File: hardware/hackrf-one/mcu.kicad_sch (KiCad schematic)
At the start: 134 parts, among them J1 USB-MICRO-B, P20 GPIO, P22 I2S, P23 DBGEN, P24 TRST, P25 LPC_ISP, P26 LPC_JTAG, P28 SD, P29 CPLD_JTAG, P3 GND, P30 BANK2_AUX, P5 LEDS, P68 SPIFI_CS, P69 VREGMODE, P70 EN_1V8, P71 ID, P72 GP_CLKIN, P73 P1_2, P74 P1_1, P75 GP_CLKIN, P76 GP_CLKIN, P77 GP_CLKIN, P78 GP_CLKIN, P79 GP_CLKIN, P80 SHIELD, P81 SPIFI_SIO2, P82 SPIFI_SIO3, Q5 MOSFET_P, SW1 DFU, SW2 RESET, U15 TVS, U20 W25Q80, U21 TPS62410, U23 LPC4320FBD144, U24 GSG-XC2C64A-7VQG100C, X2 MCU_XTAL, X3 RTC_XTAL

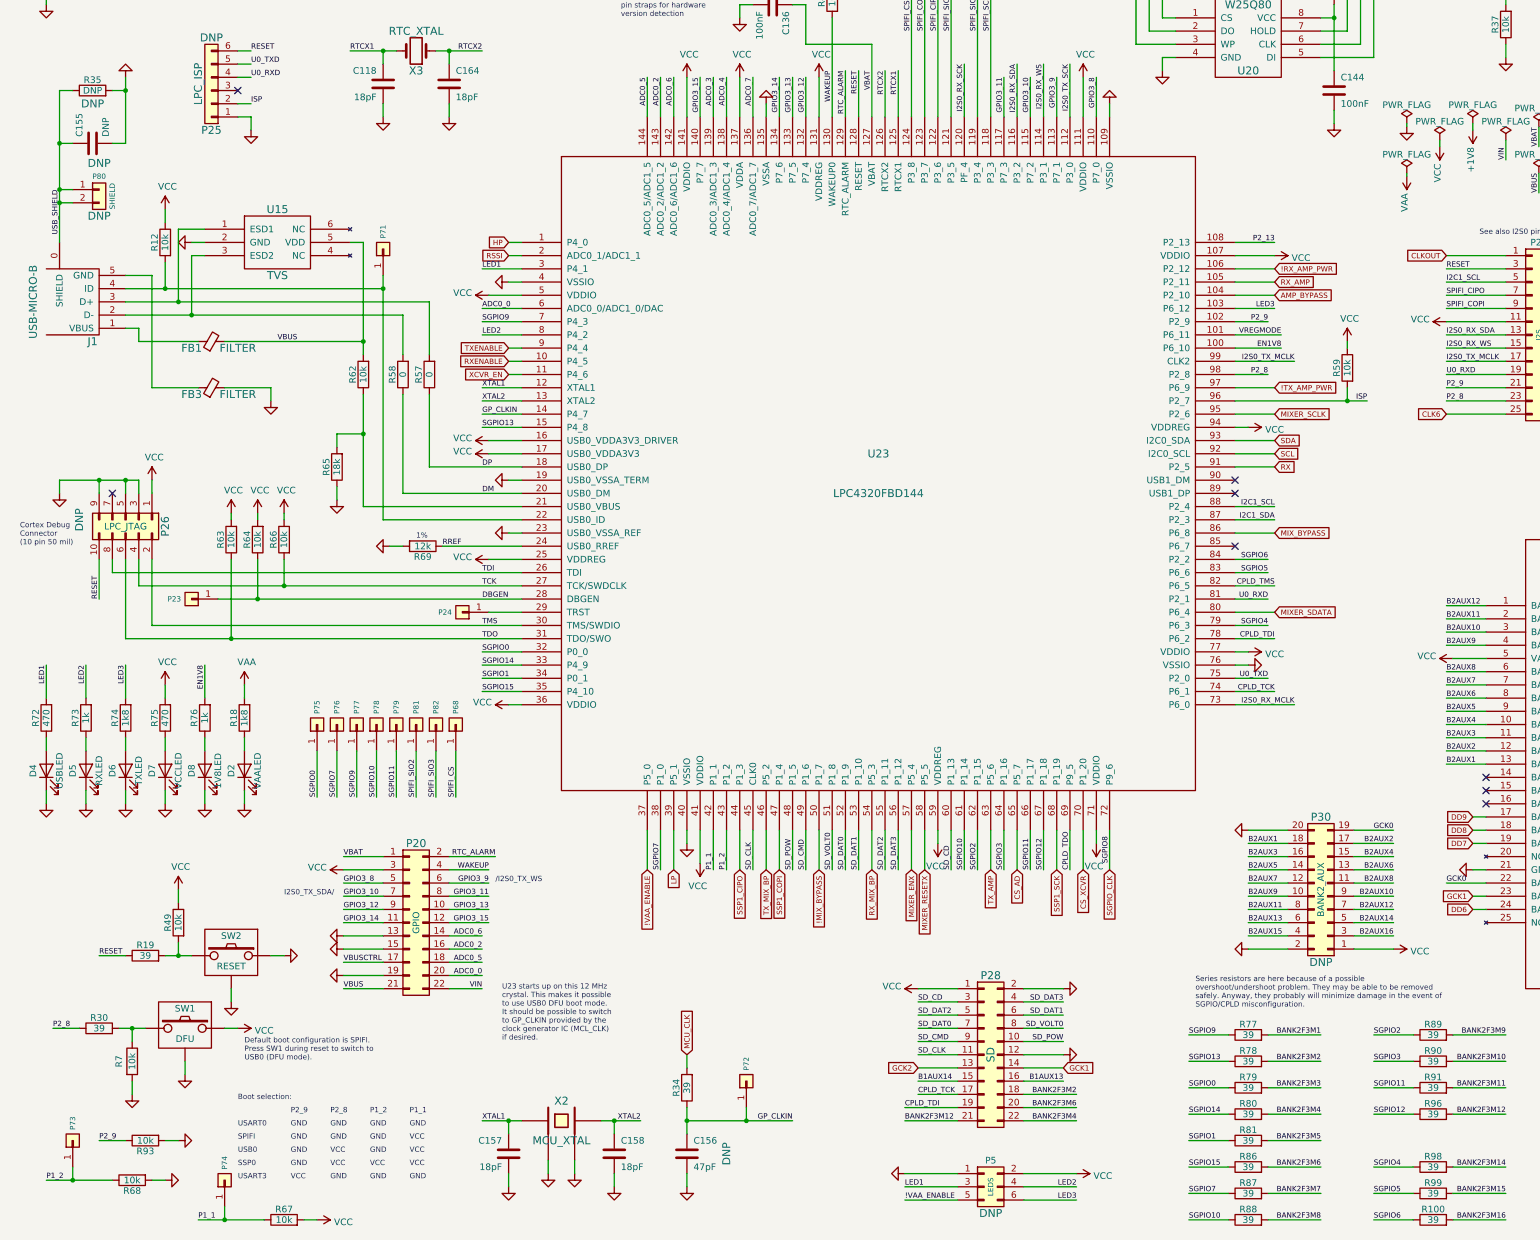
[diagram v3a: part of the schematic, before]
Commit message: HackRF One: change U19 from Si5351C to Si5351A
add clock distribution and detection
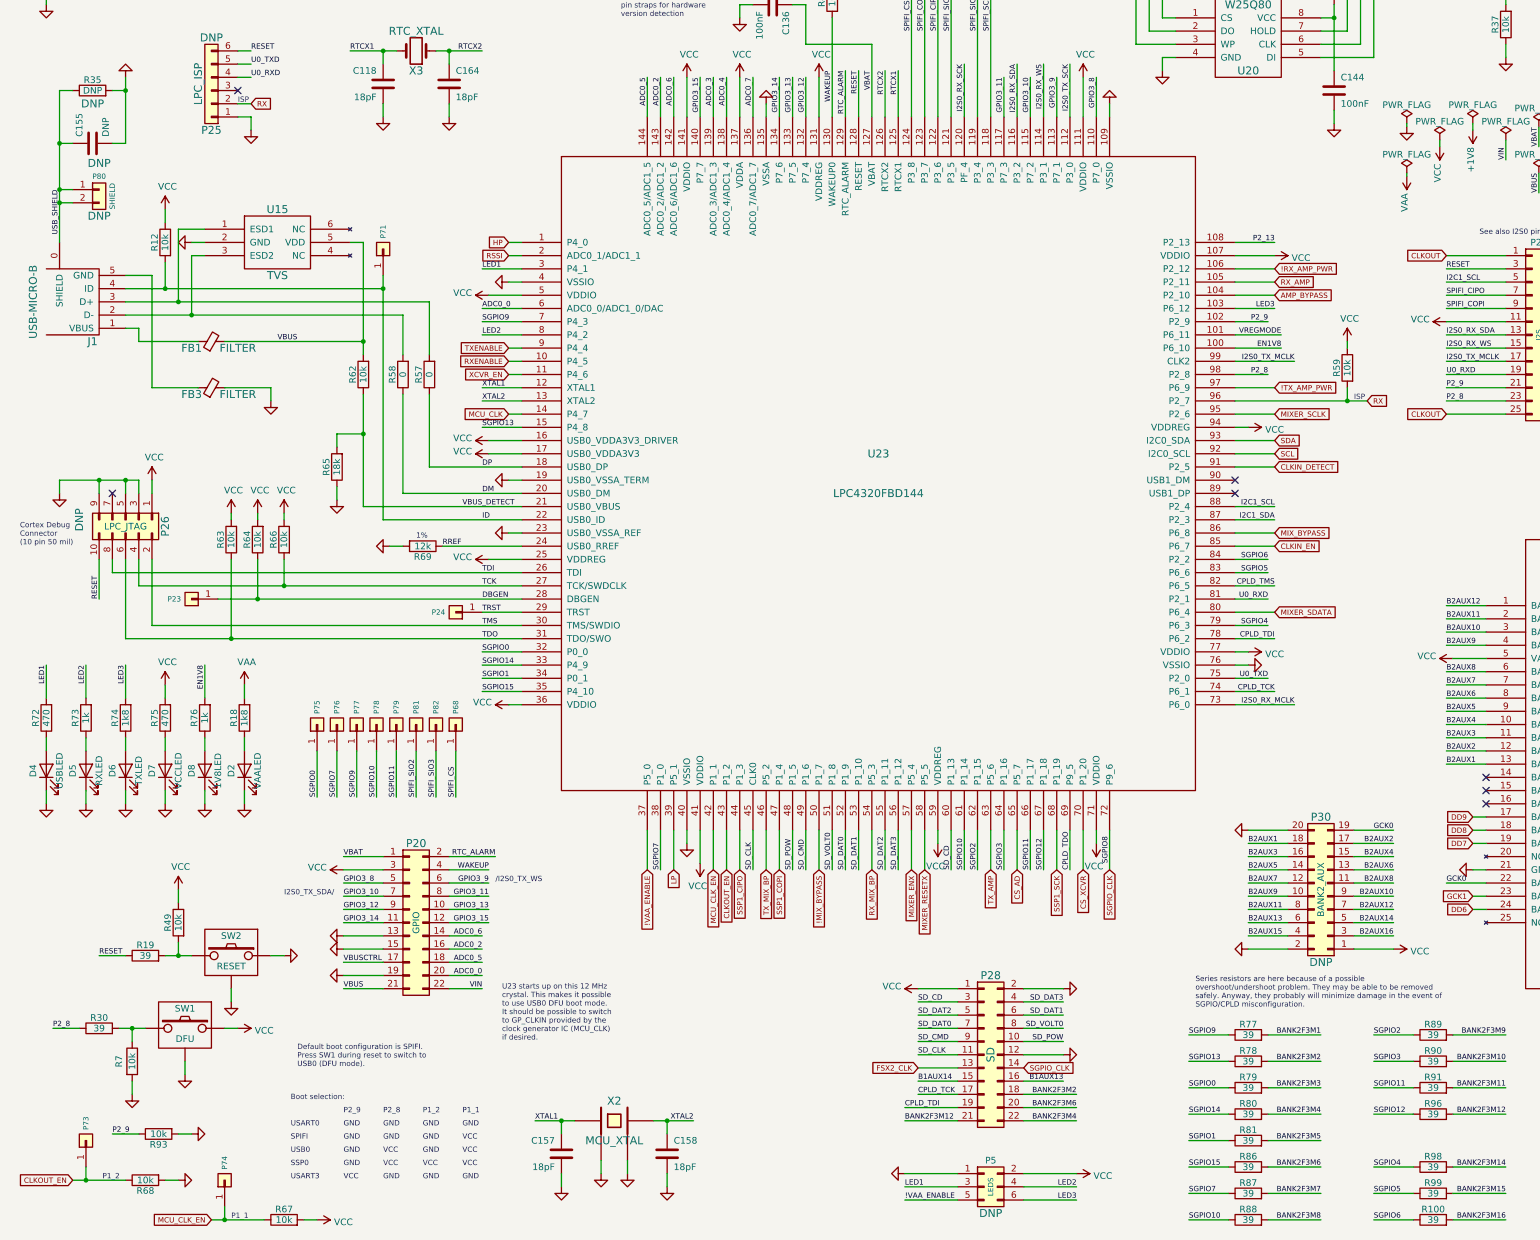
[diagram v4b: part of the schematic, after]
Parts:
- removed C156: 47pF, hackrf:GSG-0402, symbol Device:C
- removed P72: GP_CLKIN, hackrf:GSG-TESTPOINT-50MIL, symbol Connector_Generic:Conn_01x01
- removed R34: 39, hackrf:GSG-0402, symbol Device:R
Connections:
- net CLK6 is gone; now on net CLKOUT: P22.25 (Pin_25)
- net GP_CLKIN is gone; now on net MCU_CLK: U23.14 (P4_7)
- net ISP is gone; now on net RX: P25.2 (Pin_2), R59.2, U23.96 (P2_7)
- net GCK1: no longer P28.14 (Pin_14)
- net GCK2: no longer P28.13 (Pin_13)
- net RX: no longer U23.91 (P2_5)
- net SGPIO_CLK: now also P28.14 (Pin_14)
- net VBUS_DETECT: now reaches R62.1, R65.2, U23.21 (USB0_VBUS)
- net ID: now reaches J1.4 (ID), P71.1 (Pin_1), R12.2, U23.22 (USB0_ID)
- net TRST: now reaches P24.1 (Pin_1), U23.29 (TRST)
- net CLKIN_EN: now reaches U23.85 (P6_7)
- net P1_1 renamed MCU_CLK_EN
- net P1_2 renamed CLKOUT_EN
- new net CLKIN_DETECT: U23.91 (P2_5)
- new net FSX2_CLK: P28.13 (Pin_13)
- no-connect marks 15 -> 14
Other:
- note added: "ISP"
- note added: "U23 starts up on this 12 MHz crystal. This makes it possible to use USB0 DFU boot mode. It should be possible to switch to GP_CLKIN provided by the clock generator IC (MCU_CLK) if desired."
- note removed: "U23 starts up on this 12 MHz crystal. This makes it possible to use USB0 DFU boot mode. It should be possible to switch to GP_CLKIN provided by the clock generator IC (MCL_CLK) if desired."
- moved on the sheet: C157, C158, P24, P73, R68, R93, X2
